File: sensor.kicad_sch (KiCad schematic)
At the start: 12 parts, among them U4 BMI088, U5 BMI270, U6 BMP388, U7 BMM150

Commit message: Membuat library dan memperbaiki footprint pada schematic
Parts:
- U6: footprint Svayam:PQFN50P200X200X80-10N -> Svayam:XDCR_BMP388
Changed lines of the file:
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@@
 			)
 		)
-		(property "Footprint" "Svayam:PQFN50P200X200X80-10N"
+		(property "Footprint" "Svayam:XDCR_BMP388"
 			(at 53.34 118.11 0)
 			(hide yes)

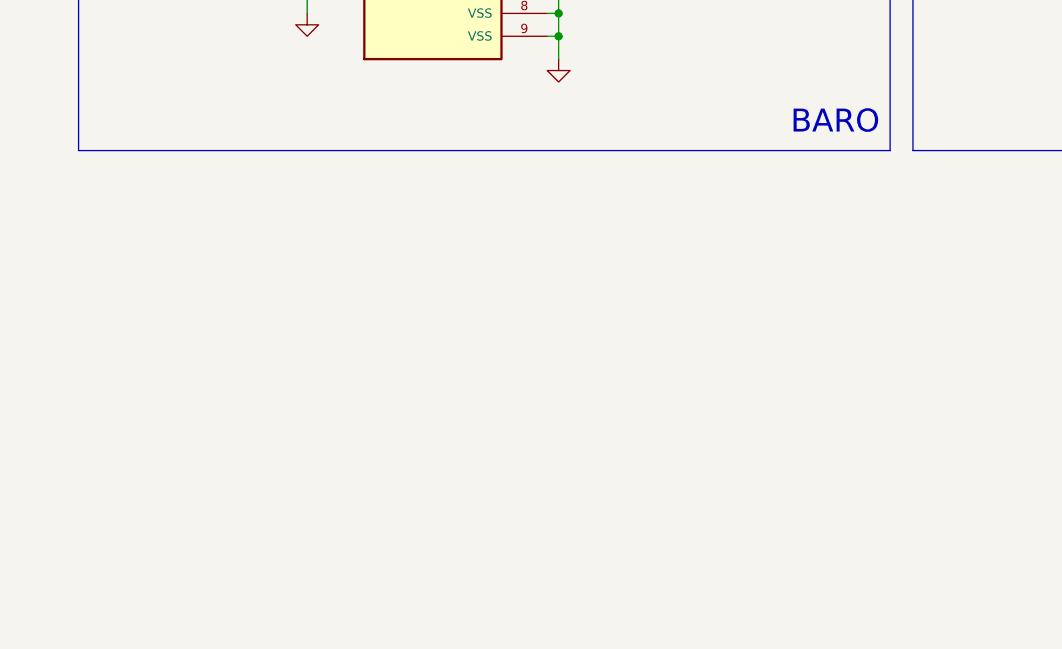
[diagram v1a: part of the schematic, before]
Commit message: Schematic: sensor redundancy + blok current limiter GPS (terverifikasi)
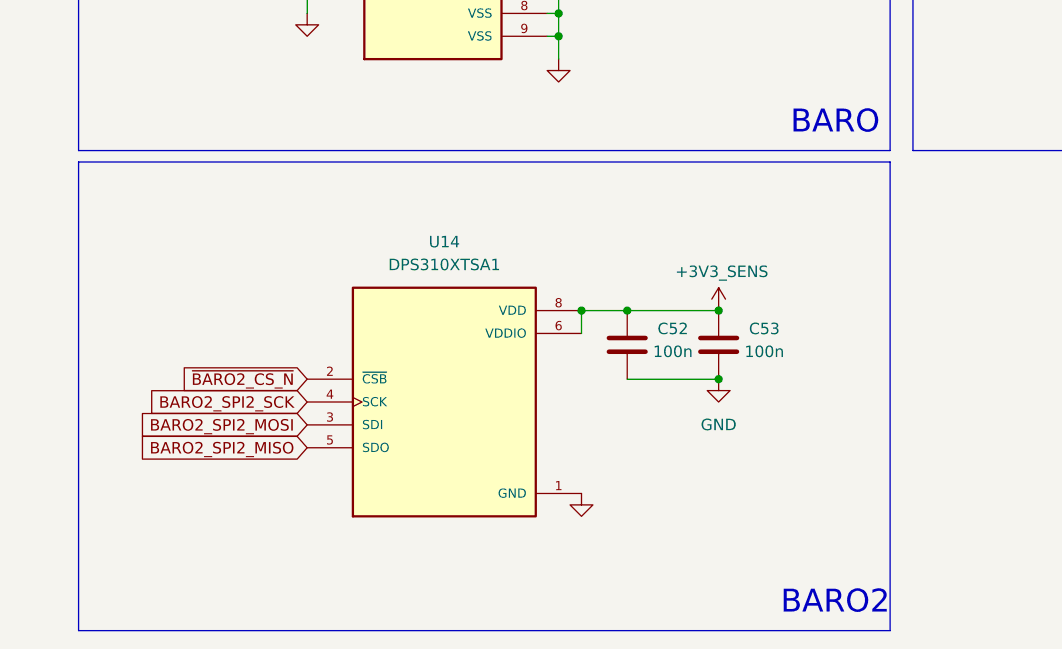
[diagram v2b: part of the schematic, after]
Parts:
- added C52, C53: 100n, Capacitor_SMD:C_0402_1005Metric, symbol Device:C
- added U14: DPS310XTSA1, DPS310XTSA1:XDCR_DPS310XTSA1, symbol Svayam_Symbol:DPS310XTSA1
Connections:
- net +3V3_SENS: now also C52.1, C53.1, U14.6 (VDDIO), U14.8 (VDD)
- net GND: now also C52.2, C53.2, U14.1 (GND), U14.7 (GND)
- new net BARO2_SPI2_MISO: U14.5 (SDO)
- new net BARO2_SPI2_MOSI: U14.3 (SDI)
- new net BARO2_SPI2_SCK: U14.4 (SCK)
- new net ~{BARO2_CS_N}: U14.2 (~{CSB})
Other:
- note added: "BARO2"

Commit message: ERC: R80 DNP+100k+fp, Pin Conflicts Map lengkap; 0 errors / 17 lib-warnings (netlist diff 0, verified)
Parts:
- U14: footprint DPS310XTSA1:XDCR_DPS310XTSA1 -> Svayam:XDCR_DPS310XTSA1
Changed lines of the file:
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@@
 			)
 		)
-		(property "Footprint" "DPS310XTSA1:XDCR_DPS310XTSA1"
+		(property "Footprint" "Svayam:XDCR_DPS310XTSA1"
 			(at 54.61 168.91 0)
 			(hide yes)

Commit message: Annotate: renumber total semua ref (Entire+Reset+X) — netlist 1009 node identik, ERC 0E/17W
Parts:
- renumbered C52 to C31, C31 to C32, C53 to C33, C26 to C34, C27 to C35, C32 to C36, C33 to C37, C28 to C38, C29 to C39, U6 to U5, U14 to U6, U4 to U7, U5 to U8, U7 to U9
